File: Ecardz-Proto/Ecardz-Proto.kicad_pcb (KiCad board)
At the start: 4 copper layers, 110 x 90 mm, 75 parts, among them IC1 M24LR04E-RMN6T/2, J1 Conn_02x06_Odd_Even, J2 Conn_01x24, J3 Conn_ARM_SWD_TagConnect_TC203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, J4 Conn_02x07_Odd_Even, Q1 NMOS, U1 STM32L071K8Ux

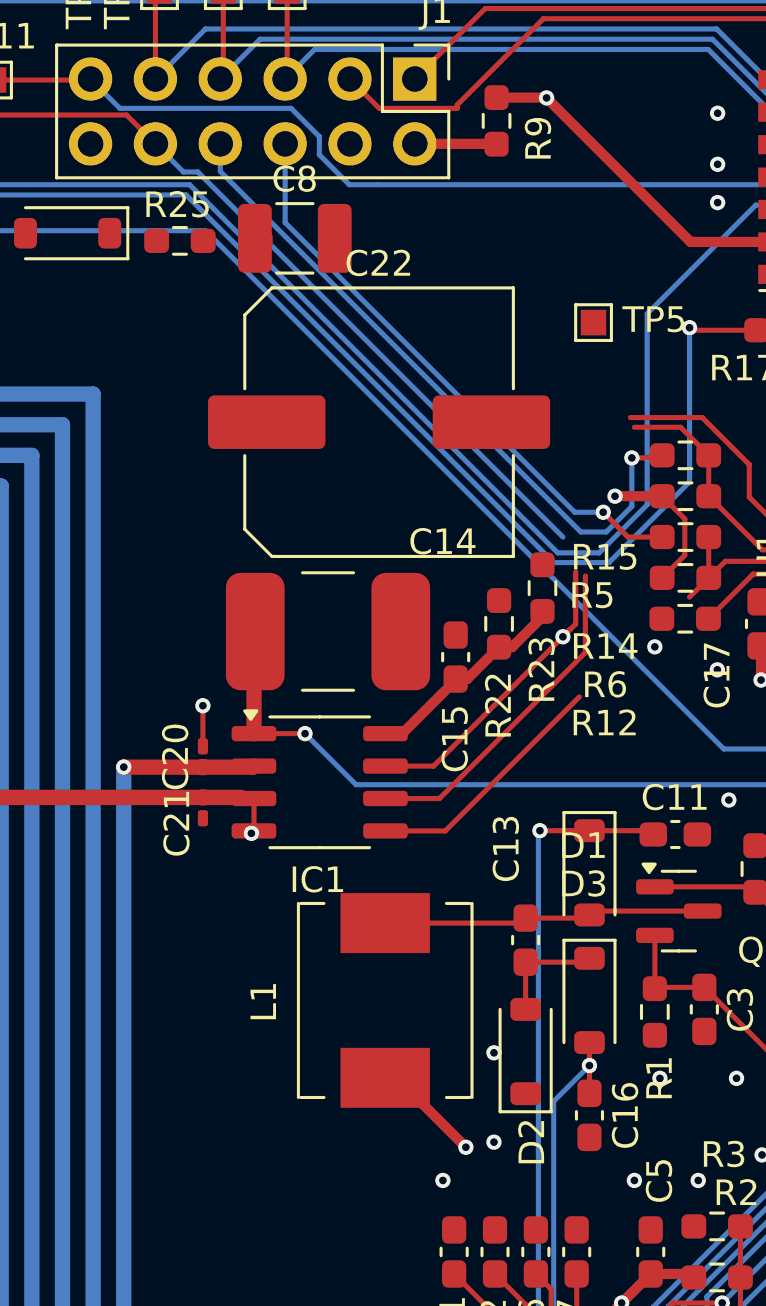
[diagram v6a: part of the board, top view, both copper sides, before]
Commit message: updated inductor
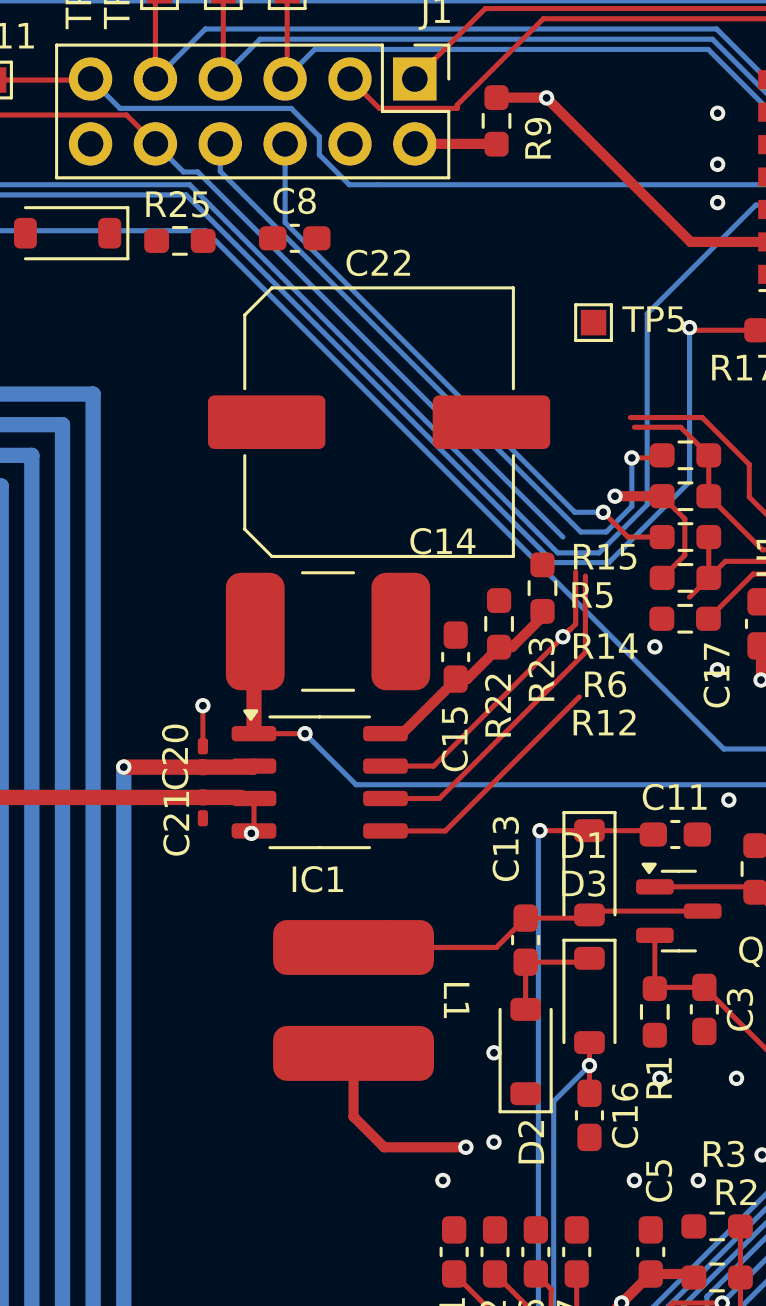
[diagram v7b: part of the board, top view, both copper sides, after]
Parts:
- C8: footprint Capacitor_SMD:C_1210_3225Metric_Pad1.33x2.70mm_HandSolder -> Capacitor_SMD:C_0603_1608Metric_Pad1.08x0.95mm_HandSolder
- L1: footprint Inductor_SMD:L_Neosid_SM-PIC0602H -> parts-lib:CDRH5D18
- moved L1 1.24 mm to (109.0, 99.5)
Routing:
- net VDD: track 181.9 -> 185.0 mm
- net Net-(D1-A): track 12.6 -> 13.4 mm

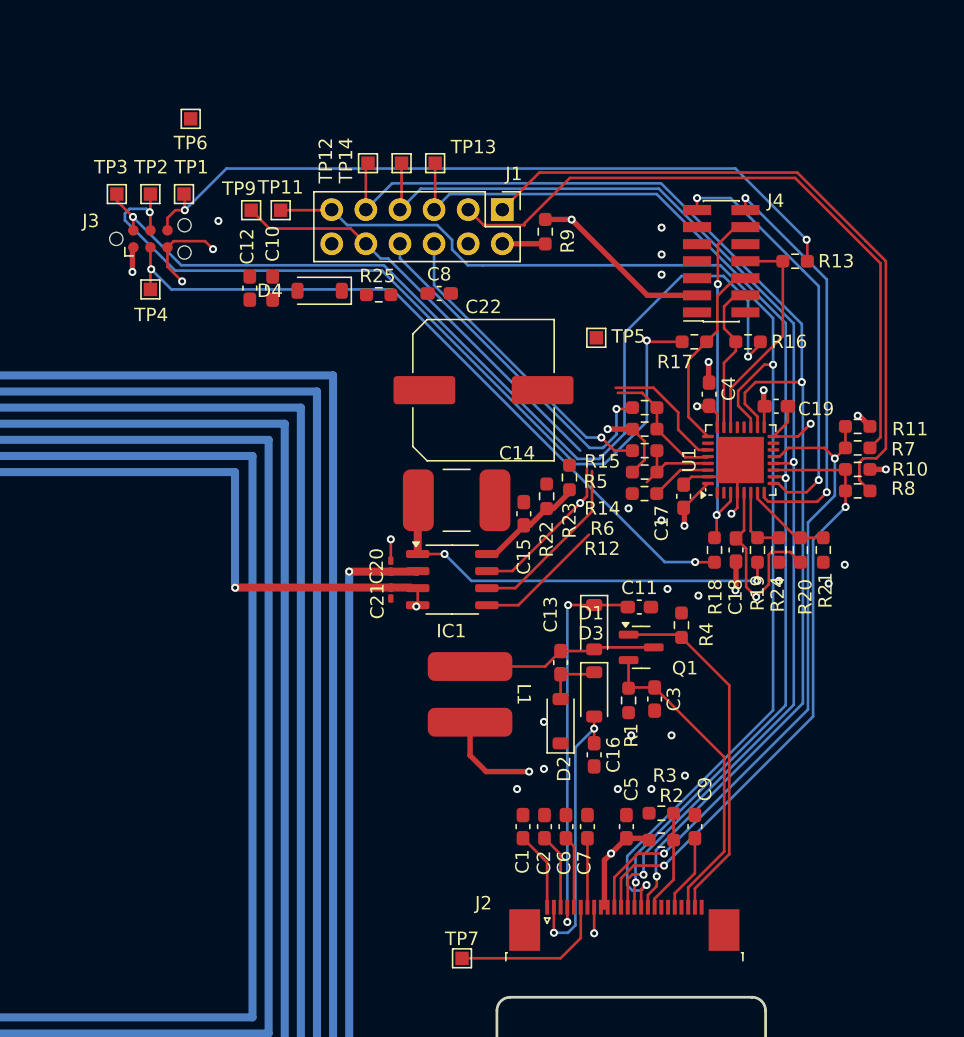
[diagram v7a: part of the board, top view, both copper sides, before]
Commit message: updated silkscreen
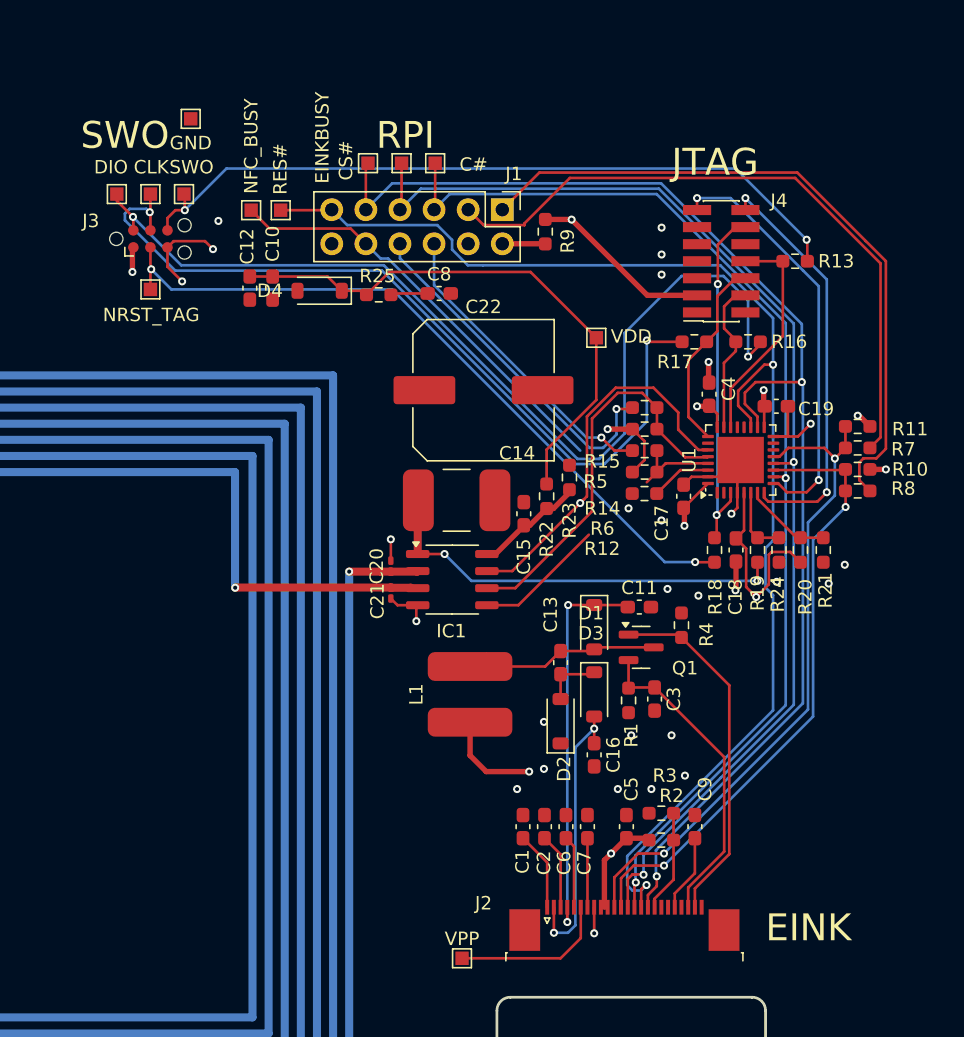
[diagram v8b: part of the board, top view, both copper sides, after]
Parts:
- renumbered TP13 to C#, TP2 to CLK, TP14 to CS#, TP3 to DIO, TP12 to EINKBUSY, TP6 to GND, TP9 to NFC_BUSY, TP4 to NRST_TAG, TP11 to RES#, TP1 to SWO, TP5 to VDD, TP7 to VPP
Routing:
- net VDD: track 185.0 -> 230.0 mm
- net /STM/NFC_BUSY: track 54.1 -> 61.0 mm
- net /STM/I2C_NFC_SCL: track 22.9 -> 29.6 mm
- net GND: track 30.4 -> 33.5 mm
- net /NFC/V_E_HARVEST: track 31.8 -> 34.5 mm
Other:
- board text added: "EINK"
- board text added: "JTAG"
- board text added: "RPI"
- board text added: "SWO"
